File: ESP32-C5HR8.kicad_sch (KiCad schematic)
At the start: 44 parts, among them IC1 ESP32-C5HR8, J2 Debug_Pins, J3 SMA PCB END LAUNCH JACK ROUND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, U14 SN74LVC1G07DBVR, U5 W25Q128JVS, Y3 ABM8W-48.0000MHZ-7-B1U-T3

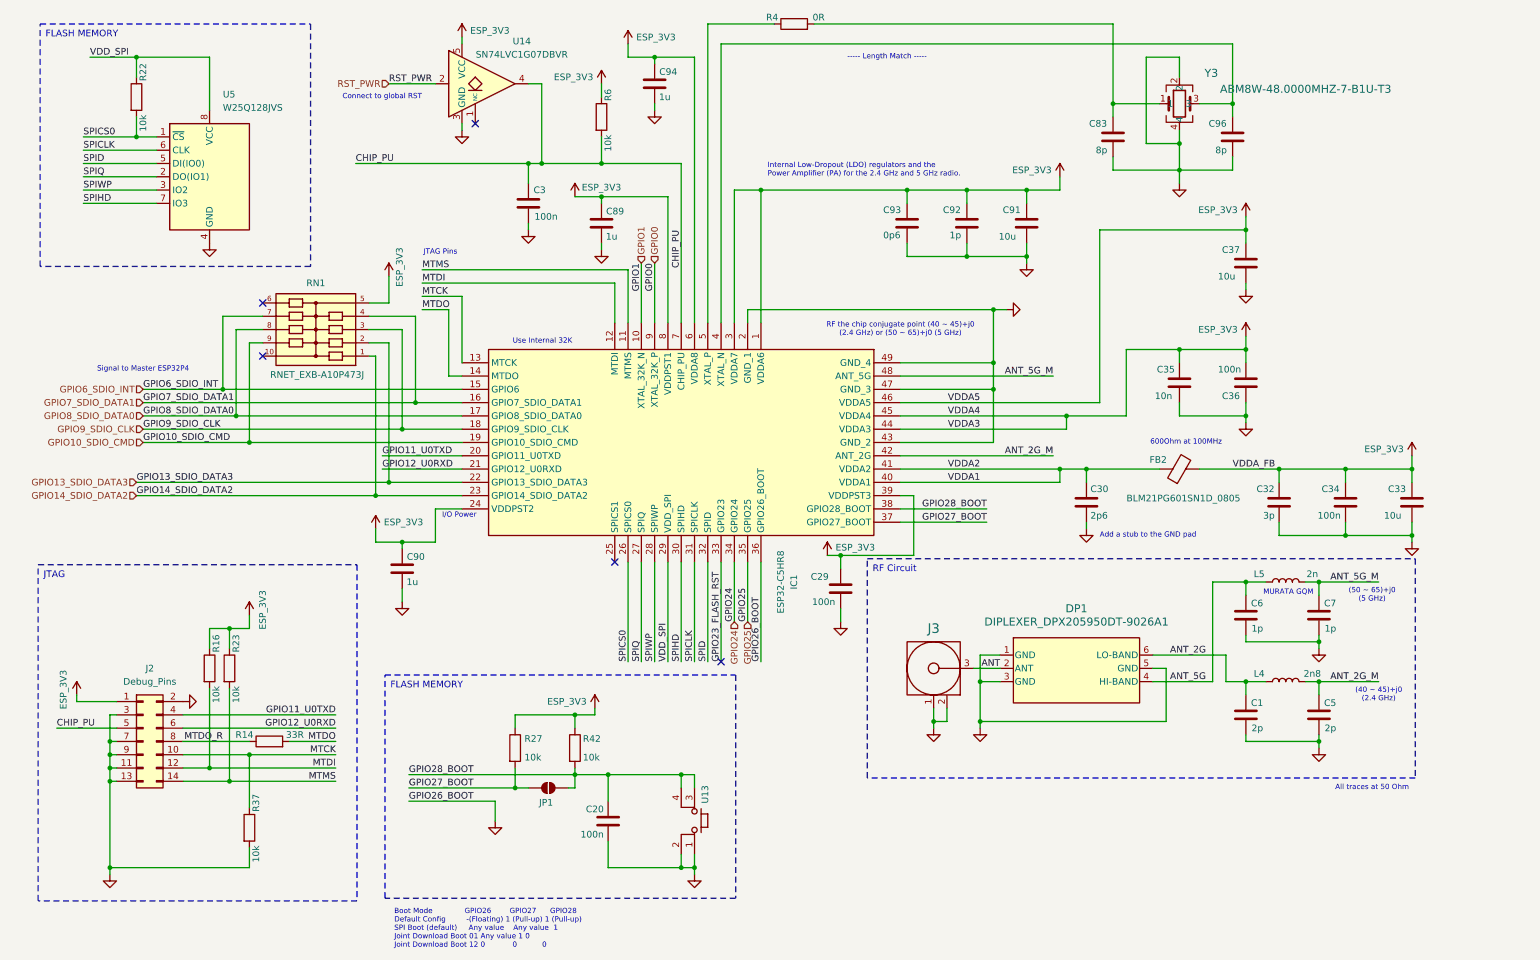
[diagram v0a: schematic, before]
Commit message: Small trace layout fixes
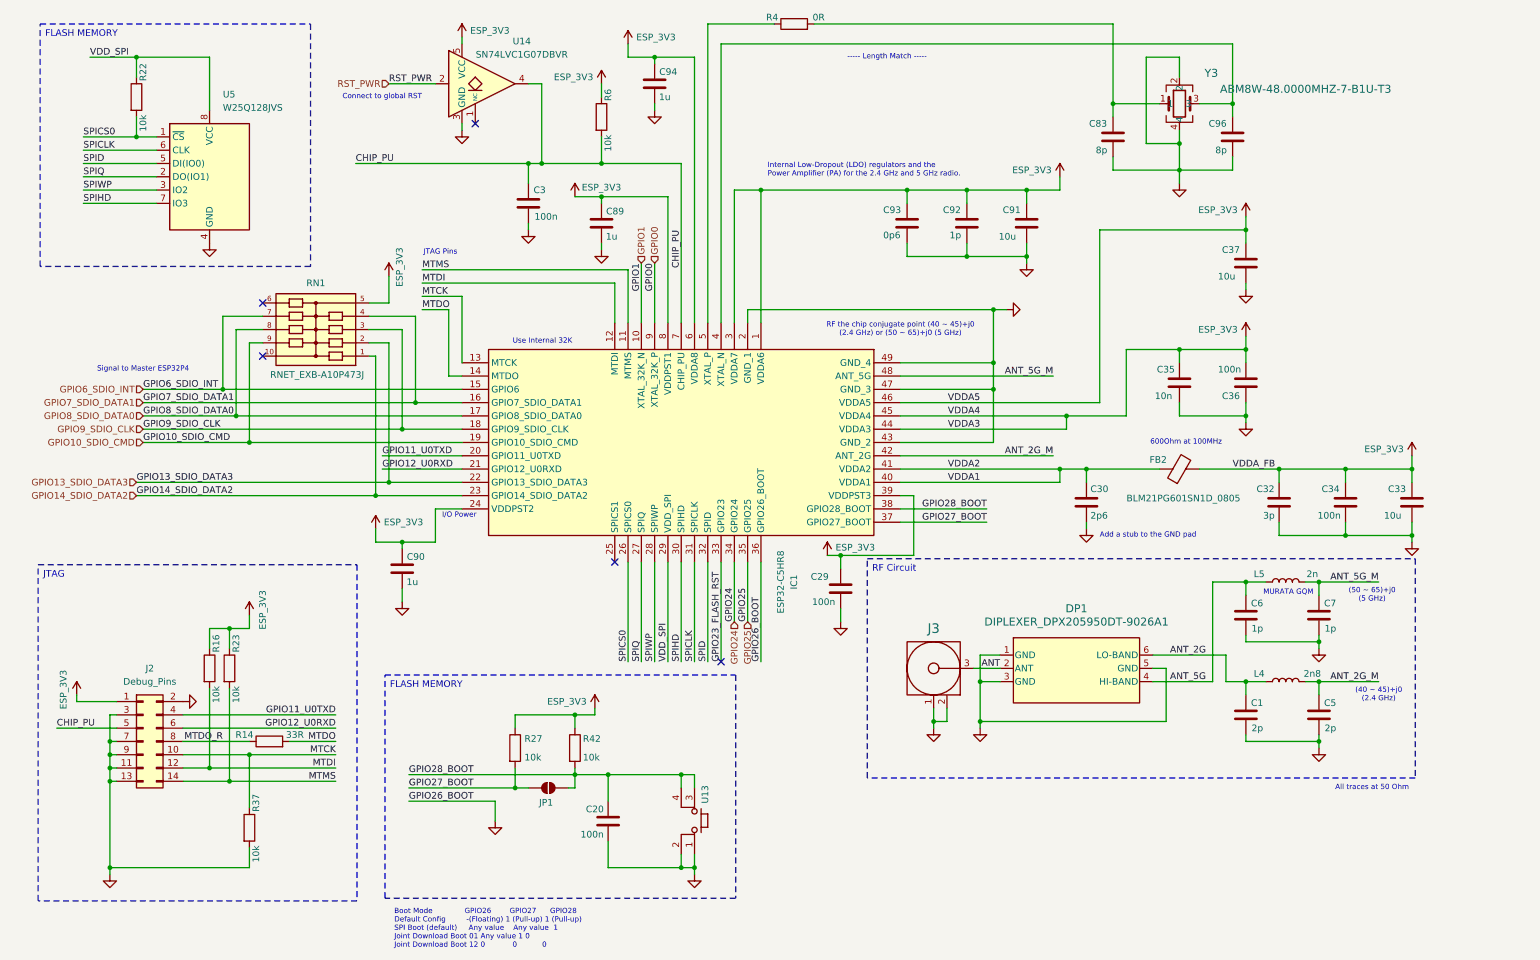
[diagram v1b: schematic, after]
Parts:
- L5: footprint Inductor_SMD:L_0603_1608Metric -> Inductor_SMD:L_0402_1005Metric_Pad0.77x0.64mm_HandSolder
- U13: value ~ -> (none)

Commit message: Power rail update
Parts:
- C32: value 3p -> 3p_GQM1875C2E3R0BB12D
- C33, C91: value 10u -> 10u_GRM188Z71A106KA73; footprint Capacitor_SMD:C_1206_3216Metric -> Capacitor_SMD:C_0603_1608Metric
- C34, C36: value 100n -> 100n_GRM188R72A104KA35
- C35: value 10n -> 10n_GRM188R72A103KA01
- C37: value 10u -> 10u_GRM188Z71A106KA73
- C92: value 1p -> 1p_GQM1875C2E1R0WB12D
- C93: value 0p6 -> 0p6_GQM1875C2ER60BB12
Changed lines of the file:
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@@
 			)
 		)
-		(property "Value" "10n"
-			(at 230.251 87.63 0)
+		(property "Value" "10n_GRM188R72A103KA01"
+			(at 228.6 90.17 0)
 			(show_name no)
 			(do_not_autoplace no)
@@
 			)
 		)
-		(property "Value" "10u"
+		(property "Value" "10u_GRM188Z71A106KA73"
 			(at 242.316 64.77 0)
 			(show_name no)
@@
 			)
 		)
-		(property "Value" "0p6"
-			(at 178.308 56.896 0)
+		(property "Value" "0p6_GQM1875C2ER60BB12"
+			(at 178.308 62.23 0)
 			(show_name no)
 			(do_not_autoplace no)
@@
 			)
 		)
-		(property "Value" "10u"
+		(property "Value" "10u_GRM188Z71A106KA73"
 			(at 200.406 57.15 0)
 			(show_name no)
@@
 			)
 		)
-		(property "Footprint" "Capacitor_SMD:C_1206_3216Metric"
+		(property "Footprint" "Capacitor_SMD:C_0603_1608Metric"
 			(at 206.7052 58.42 0)
 			(hide yes)
@@
 			)
 		)
-		(property "Value" "10u"
+		(property "Value" "10u_GRM188Z71A106KA73"
 			(at 274.066 110.49 0)
 			(show_name no)
@@
 			)
 		)
-		(property "Footprint" "Capacitor_SMD:C_1206_3216Metric"
+		(property "Footprint" "Capacitor_SMD:C_0603_1608Metric"
 			(at 280.3652 111.76 0)
 			(hide yes)
@@
 			)
 		)
-		(property "Value" "100n"
-			(at 242.316 82.55 0)
+		(property "Value" "100n_GRM188R72A104KA35"
+			(at 244.094 82.55 0)
 			(show_name no)
 			(do_not_autoplace no)
@@
 			)
 		)
-		(property "Value" "3p"
-			(at 250.952 110.49 0)
+		(property "Value" "3p_GQM1875C2E3R0BB12D"
+			(at 247.65 115.57 0)
 			(show_name no)
 			(do_not_autoplace no)
@@
 			)
 		)
-		(property "Value" "100n"
-			(at 261.366 110.49 0)
+		(property "Value" "100n_GRM188R72A104KA35"
+			(at 260.096 112.776 0)
 			(show_name no)
 			(do_not_autoplace no)
@@
 			)
 		)
-		(property "Value" "1p"
-			(at 191.008 56.896 0)
+		(property "Value" "1p_GQM1875C2E1R0WB12D"
+			(at 191.262 59.436 0)
 			(show_name no)
 			(do_not_autoplace no)

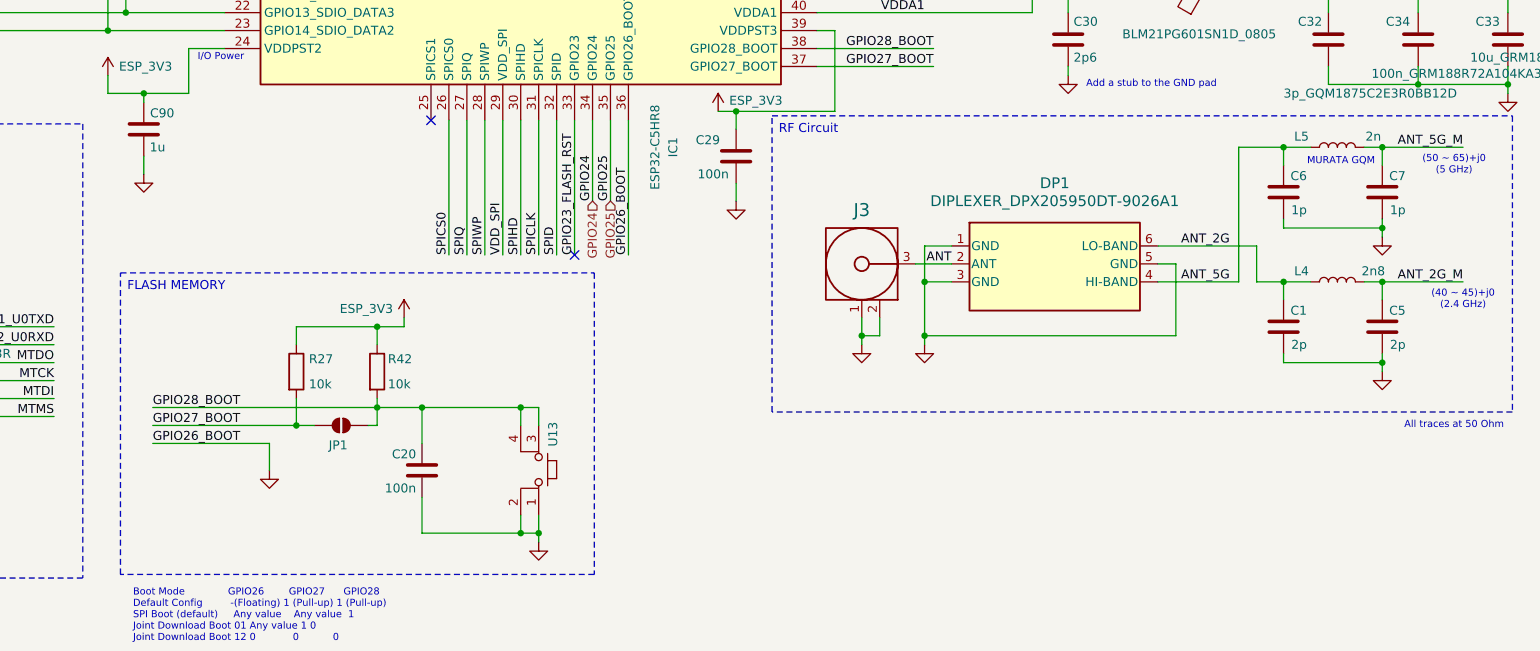
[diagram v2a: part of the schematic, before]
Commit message: Power Rail Update
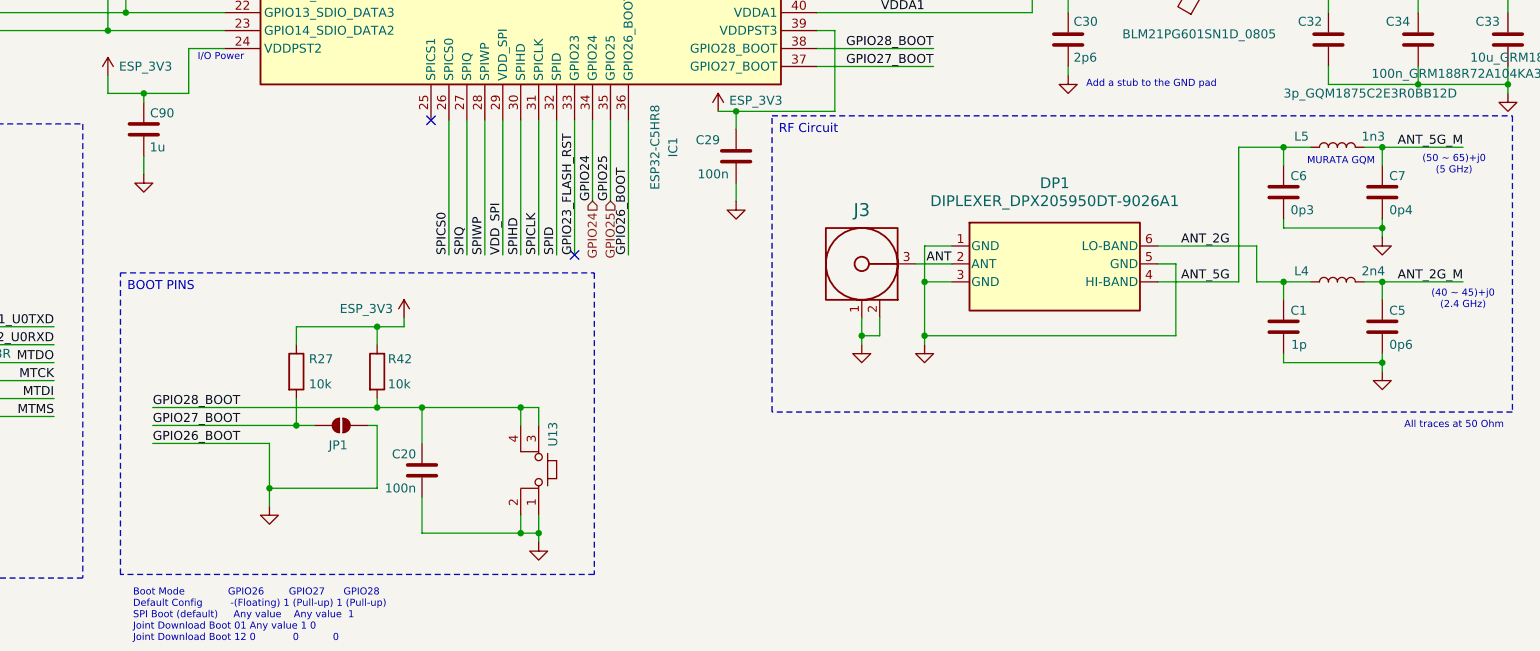
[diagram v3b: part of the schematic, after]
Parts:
- C1: value 2p -> 1p
- C5: value 2p -> 0p6
- C6: value 1p -> 0p3
- C7: value 1p -> 0p4
- L4: value 2n8 -> 2n4
- L5: value 2n -> 1n3
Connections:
- net GND: now also JP1.1 (A)
- net GPIO28_BOOT: no longer JP1.1 (A)
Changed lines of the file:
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@@
 		)
 	)
-	(text_box "FLASH MEMORY"
+	(text_box "BOOT PINS"
 		(exclude_from_sim no)
 		(at 83.058 140.97 0)
@@
 	)
 	(junction
-		(at 81.28 106.68)
+		(at 104.14 171.45)
 		(diameter 0)
 		(color 0 0 0 0)
 	)
 	(junction
-		(at 119.38 160.02)
+		(at 81.28 106.68)
 		(diameter 0)
 		(color 0 0 0 0)
@@
 	)
 	(junction
-		(at 107.95 162.56)
-		(diameter 0)
-		(color 0 0 0 0)
-	)
-	(junction
 		(at 124.46 43.18)
 		(diameter 0)
@@
 	)
 	(junction
+		(at 119.38 160.02)
+		(diameter 0)
+		(color 0 0 0 0)
+	)
+	(junction
 		(at 30.48 161.29)
 		(diameter 0)
@@
 	)
 	(junction
+		(at 107.95 162.56)
+		(diameter 0)
+		(color 0 0 0 0)
+	)
+	(junction
 		(at 213.36 91.44)
 		(diameter 0)
@@
 	(wire
 		(pts
-			(xy 119.38 160.02) (xy 125.73 160.02)
-		)
-		(stroke
-			(width 0)
-			(type default)
-		)
-	)
-	(wire
-		(pts
 			(xy 247.65 78.74) (xy 234.95 78.74)
 		)
@@
 	(wire
 		(pts
-			(xy 87.63 162.56) (xy 107.95 162.56)
+			(xy 104.14 171.45) (xy 119.38 171.45)
 		)
 		(stroke
@@
 	(wire
 		(pts
-			(xy 30.48 161.29) (xy 30.48 177.8)
+			(xy 87.63 162.56) (xy 107.95 162.56)
 		)
 		(stroke
@@
 	(wire
 		(pts
-			(xy 243.84 142.24) (xy 247.65 142.24)
+			(xy 30.48 161.29) (xy 30.48 177.8)
 		)
 		(stroke
@@
 	(wire
 		(pts
-			(xy 107.95 158.75) (xy 107.95 162.56)
+			(xy 243.84 142.24) (xy 247.65 142.24)
 		)
 		(stroke
@@
 	(wire
 		(pts
+			(xy 107.95 158.75) (xy 107.95 162.56)
+		)
+		(stroke
+			(width 0)
+			(type default)
+		)
+	)
+	(wire
+		(pts
 			(xy 279.4 114.3) (xy 266.7 114.3)
 		)
@@
 	(wire
 		(pts
-			(xy 30.48 161.29) (xy 31.75 161.29)
+			(xy 107.95 162.56) (xy 110.49 162.56)
 		)
 		(stroke
@@
 	(wire
 		(pts
-			(xy 35.56 106.68) (xy 81.28 106.68)
+			(xy 30.48 161.29) (xy 31.75 161.29)
 		)
 		(stroke
@@
 	(wire
 		(pts
-			(xy 87.63 160.02) (xy 119.38 160.02)
+			(xy 35.56 106.68) (xy 81.28 106.68)
 		)
 		(stroke
@@
 	(wire
 		(pts
-			(xy 35.56 104.14) (xy 83.82 104.14)
+			(xy 87.63 160.02) (xy 119.38 160.02)
 		)
 		(stroke
@@
 	(wire
 		(pts
-			(xy 92.71 109.22) (xy 97.79 109.22)
+			(xy 35.56 104.14) (xy 83.82 104.14)
 		)
 		(stroke
@@
 	(wire
 		(pts
-			(xy 30.48 158.75) (xy 31.75 158.75)
+			(xy 92.71 109.22) (xy 97.79 109.22)
 		)
 		(stroke
@@
 	(wire
 		(pts
-			(xy 247.65 142.24) (xy 251.46 142.24)
+			(xy 30.48 158.75) (xy 31.75 158.75)
 		)
 		(stroke
@@
 	(wire
 		(pts
-			(xy 119.38 162.56) (xy 119.38 160.02)
+			(xy 247.65 142.24) (xy 251.46 142.24)
 		)
 		(stroke
@@
 	(wire
 		(pts
-			(xy 110.49 162.56) (xy 107.95 162.56)
-		)
-		(stroke
-			(width 0)
-			(type default)
-		)
-	)
-	(wire
-		(pts
 			(xy 222.25 16.51) (xy 222.25 31.75)
 		)
@@
 	(wire
 		(pts
-			(xy 104.14 165.1) (xy 104.14 168.91)
+			(xy 104.14 165.1) (xy 104.14 171.45)
 		)
 		(stroke
@@
 	(wire
 		(pts
+			(xy 104.14 171.45) (xy 104.14 173.99)
+		)
+		(stroke
+			(width 0)
+			(type default)
+		)
+	)
+	(wire
+		(pts
 			(xy 199.39 81.28) (xy 199.39 86.36)
 		)
@@
 	(wire
 		(pts
+			(xy 119.38 158.75) (xy 119.38 160.02)
+		)
+		(stroke
+			(width 0)
+			(type default)
+		)
+	)
+	(wire
+		(pts
 			(xy 107.95 151.13) (xy 107.95 148.59)
 		)
@@
 	(wire
 		(pts
+			(xy 119.38 162.56) (xy 119.38 171.45)
+		)
+		(stroke
+			(width 0)
+			(type default)
+		)
+	)
+	(wire
+		(pts
 			(xy 194.31 60.96) (xy 205.74 60.96)
 		)
@@
 	(wire
 		(pts
-			(xy 119.38 160.02) (xy 119.38 158.75)
-		)
-		(stroke
-			(width 0)
-			(type default)
-		)
-	)
-	(wire
-		(pts
 			(xy 196.85 149.86) (xy 196.85 151.13)
 		)
@@
 	(wire
 		(pts
+			(xy 119.38 160.02) (xy 125.73 160.02)
+		)
+		(stroke
+			(width 0)
+			(type default)
+		)
+	)
+	(wire
+		(pts
 			(xy 26.67 22.86) (xy 35.56 22.86)
 		)
@@
 			)
 		)
-		(property "Value" "2n"
+		(property "Value" "1n3"
 			(at 260.35 121.666 90)
 			(show_name no)
@@
 			)
 		)
-		(property "Value" "1p"
-			(at 264.922 132.08 0)
+		(property "Value" "0p4"
+			(at 265.938 132.08 0)
 			(show_name no)
 			(do_not_autoplace no)
@@
 	(symbol
 		(lib_id "power:GND")
-		(at 104.14 168.91 0)
+		(at 104.14 173.99 0)
 		(unit 1)
 		(body_style 1)
@@
 		(fields_autoplaced yes)
 		(property "Reference" "#PWR075"
-			(at 104.14 175.26 0)
+			(at 104.14 180.34 0)
 			(hide yes)
 			(show_name no)
@@
 		)
 		(property "Value" "GND"
-			(at 104.14 173.99 0)
+			(at 104.14 179.07 0)
 			(hide yes)
 			(show_name no)
@@
 		)
 		(property "Footprint" ""
-			(at 104.14 168.91 0)
+			(at 104.14 173.99 0)
 			(hide yes)
 			(show_name no)
@@
 		)
 		(property "Datasheet" ""
-			(at 104.14 168.91 0)
+			(at 104.14 173.99 0)
 			(hide yes)
 			(show_name no)
@@
 		)
 		(property "Description" "Power symbol creates a global label with name \"GND\" , ground"
-			(at 104.14 168.91 0)
+			(at 104.14 173.99 0)
 			(hide yes)
 			(show_name no)
@@
 			)
 		)
-		(property "Value" "2p"
+		(property "Value" "1p"
 			(at 250.952 151.13 0)
 			(show_name no)
@@
 			)
 		)
-		(property "Value" "1p"
-			(at 250.952 132.08 0)
+		(property "Value" "0p3"
+			(at 251.968 132.08 0)
 			(show_name no)
 			(do_not_autoplace no)
@@
 			)
 		)
-		(property "Value" "2p"
-			(at 264.922 151.13 0)
+		(property "Value" "0p6"
+			(at 265.938 151.13 0)
 			(show_name no)
 			(do_not_autoplace no)
@@
 			)
 		)
-		(property "Value" "2n8"
+		(property "Value" "2n4"
 			(at 260.35 140.716 90)
 			(show_name no)
